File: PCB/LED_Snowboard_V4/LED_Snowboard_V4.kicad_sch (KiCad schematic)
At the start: 0 parts

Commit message: Transfer PCB To Desktop
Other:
- sheet IO and Power ports: added CELL1, CELL2, CELL3, CLK, DATA_1, DATA_2, DATA_3, DT, GATE_SIGNAL, SCL, SDA, SW, Sensor; removed none
- sheet esp32 ports: added CS, DATA_1, DATA_2, DATA_3, GATE_SIGNAL, INT, MISO, MOSI, RESET, RX, SCL, SCLK, SDA, SD_SW, SENSOR, TX; removed none
- sheet peripherals ports: added CS, INT, MISO, MOSI, RX, SCL, SCLK, SDA, SD_SW, TX; removed none
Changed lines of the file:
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@@
       (effects (font (size 1.27 1.27)) (justify left top))
+    )
+    (pin "INT" input (at 196.85 53.34 180)
+      (effects (font (size 1.27 1.27)) (justify left))
+    )
+    (pin "SD_SW" input (at 196.85 59.69 180)
+      (effects (font (size 1.27 1.27)) (justify left))
+    )
+    (pin "SCLK" input (at 196.85 66.04 180)
+      (effects (font (size 1.27 1.27)) (justify left))
+    )
+    (pin "CS" input (at 196.85 71.12 180)
+      (effects (font (size 1.27 1.27)) (justify left))
+    )
+    (pin "MOSI" input (at 196.85 74.93 180)
+      (effects (font (size 1.27 1.27)) (justify left))
+    )
+    (pin "MISO" input (at 196.85 78.74 180)
+      (effects (font (size 1.27 1.27)) (justify left))
+    )
+    (pin "TX" input (at 196.85 83.82 180)
+      (effects (font (size 1.27 1.27)) (justify left))
+    )
+    (pin "RX" input (at 196.85 88.9 180)
+      (effects (font (size 1.27 1.27)) (justify left))
+    )
+    (pin "SDA" input (at 196.85 91.44 180)
+      (effects (font (size 1.27 1.27)) (justify left))
+    )
+    (pin "SCL" input (at 196.85 93.98 180)
+      (effects (font (size 1.27 1.27)) (justify left))
     )
     (instances
@@
       (effects (font (size 1.27 1.27)) (justify left top))
     )
+    (pin "Sensor" input (at 111.76 54.61 0)
+      (effects (font (size 1.27 1.27)) (justify right))
+    )
+    (pin "DATA_2" input (at 111.76 57.15 0)
+      (effects (font (size 1.27 1.27)) (justify right))
+    )
+    (pin "DATA_3" input (at 111.76 60.96 0)
+      (effects (font (size 1.27 1.27)) (justify right))
+    )
+    (pin "DATA_1" input (at 111.76 63.5 0)
+      (effects (font (size 1.27 1.27)) (justify right))
+    )
+    (pin "CLK" input (at 111.76 66.04 0)
+      (effects (font (size 1.27 1.27)) (justify right))
+    )
+    (pin "SW" input (at 111.76 69.85 0)
+      (effects (font (size 1.27 1.27)) (justify right))
+    )
+    (pin "DT" input (at 111.76 73.66 0)
+      (effects (font (size 1.27 1.27)) (justify right))
+    )
+    (pin "GATE_SIGNAL" input (at 111.76 77.47 0)
+      (effects (font (size 1.27 1.27)) (justify right))
+    )
+    (pin "CELL1" input (at 111.76 80.01 0)
+      (effects (font (size 1.27 1.27)) (justify right))
+    )
+    (pin "CELL2" input (at 111.76 83.82 0)
+      (effects (font (size 1.27 1.27)) (justify right))
+    )
+    (pin "CELL3" input (at 111.76 88.9 0)
+      (effects (font (size 1.27 1.27)) (justify right))
+    )
+    (pin "SCL" input (at 111.76 92.71 0)
+      (effects (font (size 1.27 1.27)) (justify right))
+    )
+    (pin "SDA" input (at 111.76 96.52 0)
+      (effects (font (size 1.27 1.27)) (justify right))
+    )
     (instances
       (project "LED_Snowboard_V4"
@@
       (effects (font (size 1.27 1.27)) (justify left top))
     )
+    (pin "DATA_1" input (at 130.81 55.88 180)
+      (effects (font (size 1.27 1.27)) (justify left))
+    )
+    (pin "GATE_SIGNAL" input (at 130.81 59.69 180)
+      (effects (font (size 1.27 1.27)) (justify left))
+    )
+    (pin "DATA_2" input (at 130.81 63.5 180)
+      (effects (font (size 1.27 1.27)) (justify left))
+    )
+    (pin "DATA_3" input (at 130.81 67.31 180)
+      (effects (font (size 1.27 1.27)) (justify left))
+    )
+    (pin "INT" input (at 130.81 71.12 180)
+      (effects (font (size 1.27 1.27)) (justify left))
+    )
+    (pin "SENSOR" input (at 130.81 74.93 180)
+      (effects (font (size 1.27 1.27)) (justify left))
+    )
+    (pin "RESET" input (at 130.81 77.47 180)
+      (effects (font (size 1.27 1.27)) (justify left))
+    )
+    (pin "SD_SW" input (at 130.81 81.28 180)
+      (effects (font (size 1.27 1.27)) (justify left))
+    )
+    (pin "SDA" input (at 130.81 85.09 180)
+      (effects (font (size 1.27 1.27)) (justify left))
+    )
+    (pin "SCL" input (at 130.81 90.17 180)
+      (effects (font (size 1.27 1.27)) (justify left))
+    )
+    (pin "MOSI" input (at 130.81 93.98 180)
+      (effects (font (size 1.27 1.27)) (justify left))
+    )
+    (pin "SCLK" input (at 130.81 99.06 180)
+      (effects (font (size 1.27 1.27)) (justify left))
+    )
+    (pin "MISO" input (at 130.81 106.68 180)
+      (effects (font (size 1.27 1.27)) (justify left))
+    )
+    (pin "CS" input (at 130.81 111.76 180)
+      (effects (font (size 1.27 1.27)) (justify left))
+    )
+    (pin "RX" input (at 130.81 114.3 180)
+      (effects (font (size 1.27 1.27)) (justify left))
+    )
+    (pin "TX" input (at 130.81 115.57 180)
+      (effects (font (size 1.27 1.27)) (justify left))
+    )
     (instances

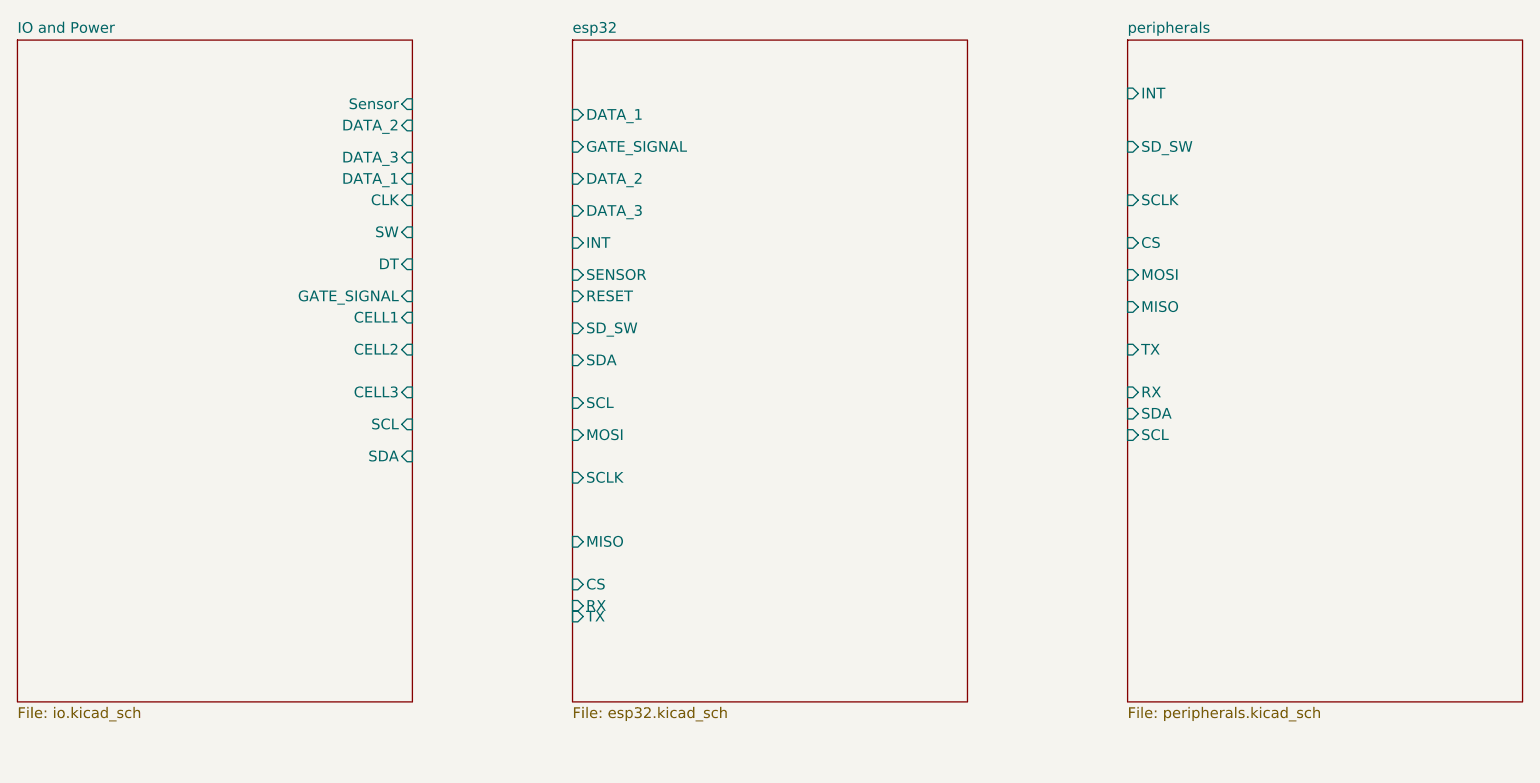
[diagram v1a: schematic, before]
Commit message: Post Review
Reviewed with Tim. need to add power line protections. settled on no battery heater for now
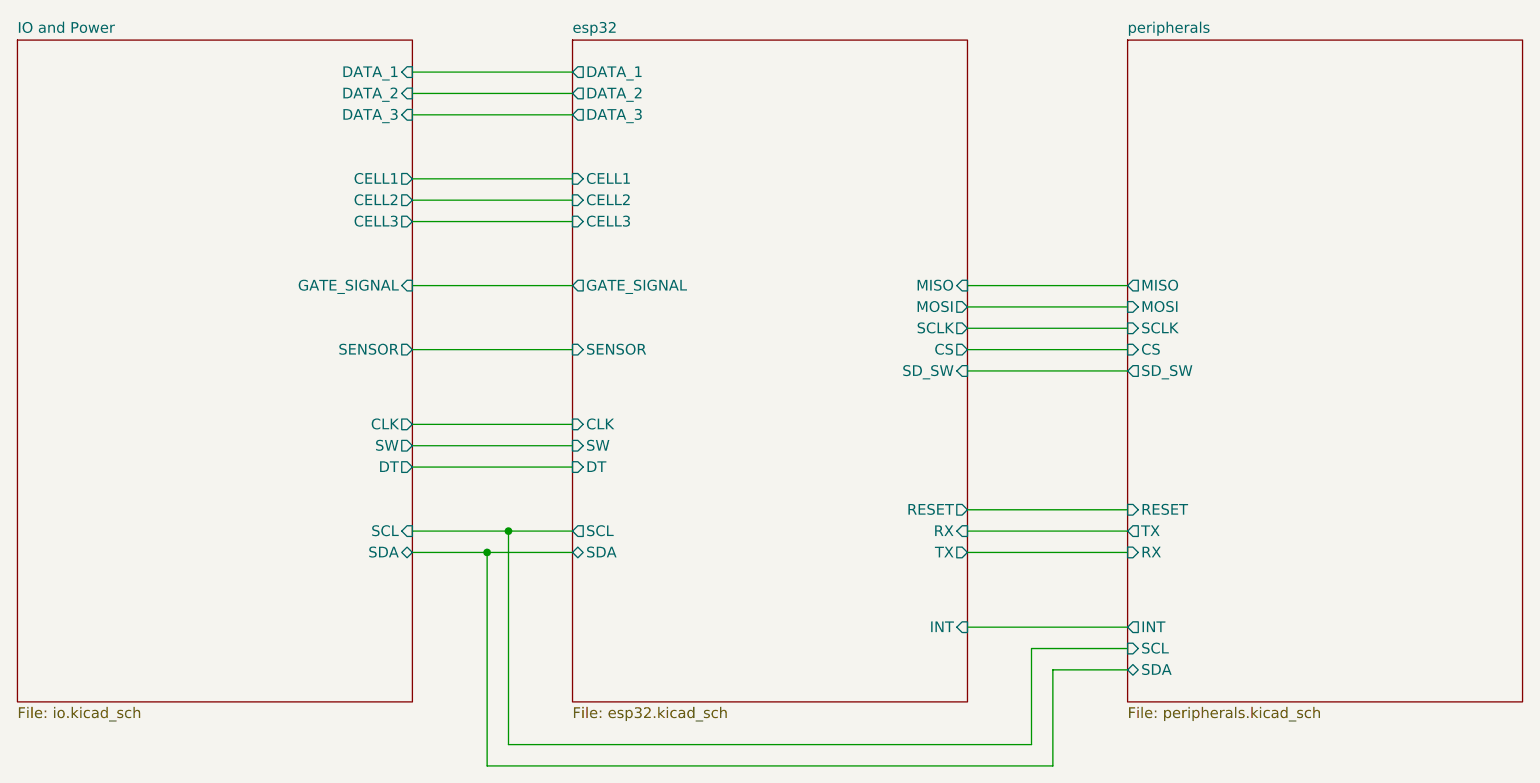
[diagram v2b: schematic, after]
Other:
- sheet IO and Power ports: added SENSOR; removed Sensor
- sheet esp32 ports: added CELL1, CELL2, CELL3, CLK, DT, SW; removed none
- sheet peripherals ports: added RESET; removed none
